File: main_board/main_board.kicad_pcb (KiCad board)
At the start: 2 copper layers, 80 x 80 mm, 103 parts, among them J10 B5B-XH, J11 B5B-XH, J12 B3B-XH, J13 B5B-XH, J2 Conn_01x02, J3 Conn_01x02, J4 EncSide, J5 MainSide, J6 EncSide, J7 MainSide, J8 Conn_01x02, J9 Conn_01x02, Q1 ST-1KL3A, Q10 DTC114E, Q2 ST-1KL3A, Q3 ST-1KL3A, Q4 ST-1KL3A, Q5 IRLML6344, Q6 IRLML6344, Q7 IRLML6344, Q8 IRLML6344, Q9 DTC114E, U1 ADCS7476, U10 AS5047D, U11 LSM6DSR, U12 OKL-T/6-W12N-C, U13 XC6221B302GR, U14 FT232RL, U15 SL2.1A, U2 BD63573NUV, U3 ADCS7476, U4 ADCS7476, U5 BD63573NUV, U6 ESP32-S3-PICO-1-N8R2, U7 AS5047D, U8 ADCS7476, U9 ADCS7476, Y1 12MHz

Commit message: アートワーク : 部品配置
Signed-off-by: Kazuki Iida <elkel53930@gmail.com>
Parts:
- D4, D5: footprint Library:SFH4550 -> Library:SFH4550_Mirror
- Q1, Q2: footprint Library:ST-1KL3A -> Library:ST-1KL3A_Mirror
- moved U9 186.0 mm to (215.0, 65.0), turned to 90 degrees
- moved C15 183.6 mm to (198.2, 140.5)
- moved C20 181.1 mm to (220.0, 75.5)
- moved C11 179.3 mm to (215.0, 68.0)
- moved C13 178.8 mm to (215.0, 69.5), turned to 180 degrees
- moved U1 178.1 mm to (207.0, 50.0), turned to 90 degrees
- moved C1 173.7 mm to (207.0, 53.0)
- moved C2 173.7 mm to (207.0, 54.5), turned to 180 degrees
- moved R10 170.3 mm to (215.0, 72.5), turned to 180 degrees
- moved R14 168.0 mm to (215.0, 74.0)
- moved R3 167.9 mm to (209.5, 53.0), turned to -90 degrees
- moved R18 165.3 mm to (215.0, 57.0)
- moved R5 164.0 mm to (209.5, 50.0), turned to -90 degrees
- moved U8 163.9 mm to (193.0, 54.5), turned to -90 degrees
- moved Q8 160.9 mm to (215.0, 60.0), turned to -90 degrees
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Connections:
- C31 pad 1: /Power/CHIP_PU -> CHIP_PU
- C33 pad 1: /Power/GPIO0 -> GPIO0
- Q10 pad 3: /Power/GPIO0 -> GPIO0
- Q9 pad 3: /Power/CHIP_PU -> CHIP_PU
- R1 pad 1: Net-(D1-K) -> /LED_0
- R1 pad 2: /LED_0 -> Net-(D1-K)
- R6 pad 1: /CHIP_PU -> CHIP_PU
- U14 pad 1: /Power/RXD0 -> RXD0
- U14 pad 5: /Power/TXD0 -> TXD0
- U6 pad 24: /CS_ENC_L -> /LED_1
- U6 pad 25: /CS_ENC_R -> unconnected-(U6-GPIO19-Pad25)
- U6 pad 38: /LED_1 -> /PWM_L
- U6 pad 39: /PWM_L -> /CWCCW_L
- U6 pad 4: /CHIP_PU -> CHIP_PU
- U6 pad 40: /CWCCW_L -> /CS_ENC_L
- U6 pad 41: /PWM_R -> /CS_ENC_R
- U6 pad 42: /CWCCW_R -> /PWM_R
- U6 pad 43: unconnected-(U6-GPIO38-Pad43) -> /CWCCW_R
- U6 pad 49: /TXD -> TXD0
- U6 pad 5: /GPIO0 -> GPIO0
- U6 pad 50: /RXD -> RXD0

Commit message: アートワーク : 部品配置完了
Signed-off-by: Kazuki Iida <elkel53930@gmail.com>
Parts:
- added G***: LOGO, Library:AMacLogo, F.Cu at (158.0, 44.5)
- added H1: M3 mounting hole, MountingHole:MountingHole_3.2mm_M3, F.Cu at (184.0, 116.5)
- added H10: M2 mounting hole, MountingHole:MountingHole_2.2mm_M2, F.Cu at (145.8, 82.8)
- added H11: M2 mounting hole, MountingHole:MountingHole_2.2mm_M2, F.Cu at (151.2, 82.8)
- added H2: M3 mounting hole, MountingHole:MountingHole_3.2mm_M3, F.Cu at (160.5, 61.3)
- added H3: M3 mounting hole, MountingHole:MountingHole_3.2mm_M3, F.Cu at (207.5, 61.3)
- added H4: M2 mounting hole, MountingHole:MountingHole_2.2mm_M2, F.Cu at (222.2, 95.2)
- added H5: M2 mounting hole, MountingHole:MountingHole_2.2mm_M2, F.Cu at (216.8, 95.2)
- added H6: M2 mounting hole, MountingHole:MountingHole_2.2mm_M2, F.Cu at (222.2, 82.8)
- added H7: M2 mounting hole, MountingHole:MountingHole_2.2mm_M2, F.Cu at (216.8, 82.8)
- added H8: M2 mounting hole, MountingHole:MountingHole_2.2mm_M2, F.Cu at (145.8, 95.2)
- added H9: M2 mounting hole, MountingHole:MountingHole_2.2mm_M2, F.Cu at (151.2, 95.2)
- moved C15 54.6 mm to (216.5, 89.0), turned to -90 degrees
- moved C16 53.7 mm to (151.5, 89.0), turned to -90 degrees
- moved D3 52.4 mm to (202.0, 83.5), turned to 90 degrees
- moved R2 51.0 mm to (202.0, 80.5), turned to 90 degrees
- moved U10 44.8 mm to (148.0, 89.0), turned to 90 degrees
- moved U7 43.8 mm to (220.0, 89.0), turned to 90 degrees
- moved J6 41.2 mm to (148.5, 100.0), turned to 180 degrees
- moved J4 39.7 mm to (219.5, 100.0), turned to 180 degrees
- moved R1 34.4 mm to (190.0, 62.0)
- moved D1 34.0 mm to (193.0, 62.0)
- moved R4 30.2 mm to (190.0, 60.5), turned to 180 degrees
- moved D2 30.1 mm to (193.0, 60.5)
- moved R6 14.3 mm to (183.0, 83.0), turned to 0 degrees
- moved C8 12.6 mm to (178.0, 63.5), turned to 0 degrees
- moved C23 4.00 mm to (189.0, 73.0)
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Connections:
- C15 pad 2: Net-(J4-Pin_6) -> Net-(J4-Pin_2)
- C16 pad 2: Net-(J6-Pin_6) -> Net-(J6-Pin_2)
- J5 pad 2: /SPI1_MOSI -> GND
- J5 pad 3: /SPI1_MISO -> /SPI1_MOSI
- J5 pad 4: /SPI1_SCK -> /SPI1_MISO
- J5 pad 5: /CS_ENC_L -> /SPI1_SCK
- J5 pad 6: GND -> /CS_ENC_L
- J7 pad 2: /SPI1_MOSI -> GND
- J7 pad 3: /SPI1_MISO -> /SPI1_MOSI
- J7 pad 4: /SPI1_SCK -> /SPI1_MISO
- J7 pad 5: /CS_ENC_R -> /SPI1_SCK
- J7 pad 6: GND -> /CS_ENC_R
- U10 pad 1: Net-(J6-Pin_5) -> Net-(J6-Pin_6)
- U10 pad 13: Net-(J6-Pin_6) -> Net-(J6-Pin_2)
- U10 pad 2: Net-(J6-Pin_4) -> Net-(J6-Pin_5)
- U10 pad 3: Net-(J6-Pin_3) -> Net-(J6-Pin_4)
- U10 pad 4: Net-(J6-Pin_2) -> Net-(J6-Pin_3)
- U10 pad 5: Net-(J6-Pin_6) -> Net-(J6-Pin_2)
- U6 pad 10: /LS_EN -> /SPI2_SCK
- U6 pad 11: /CS_BATT -> /CS_IMU
- U6 pad 12: /SPI2_MISO -> /PWM_R
- U6 pad 13: /SPI2_MOSI -> /CWCCW_R
- U6 pad 14: /SPI2_SCK -> /SPI1_MOSI
- U6 pad 15: /CS_IMU -> /SPI1_MISO
- U6 pad 16: /CS_LF -> /SPI1_SCK
- U6 pad 17: /LF_EN -> /CS_ENC_L
- U6 pad 18: /SPI1_MOSI -> /CS_ENC_R
- U6 pad 19: /SPI1_MISO -> /LED_0
- U6 pad 23: /SPI1_SCK -> /LED_1
- U6 pad 24: /LED_1 -> /CS_RF
- U6 pad 27: /LED_0 -> /RF_EN
- U6 pad 38: /PWM_L -> /CS_BATT
- U6 pad 39: /CWCCW_L -> /CS_RS
- U6 pad 40: /CS_ENC_L -> /RS_EN
- U6 pad 41: /CS_ENC_R -> /CS_LS
- U6 pad 42: /PWM_R -> /LS_EN
- U6 pad 43: /CWCCW_R -> /CS_LF
- U6 pad 52: /CS_RF -> /LF_EN
- U6 pad 6: /RF_EN -> /CWCCW_L
- U6 pad 7: /CS_RS -> /PWM_L
- U6 pad 8: /RS_EN -> /SPI2_MISO
- U6 pad 9: /CS_LS -> /SPI2_MOSI
- U7 pad 1: Net-(J4-Pin_5) -> Net-(J4-Pin_6)
- U7 pad 13: Net-(J4-Pin_6) -> Net-(J4-Pin_2)
- U7 pad 2: Net-(J4-Pin_4) -> Net-(J4-Pin_5)
- U7 pad 3: Net-(J4-Pin_3) -> Net-(J4-Pin_4)
- U7 pad 4: Net-(J4-Pin_2) -> Net-(J4-Pin_3)
- U7 pad 5: Net-(J4-Pin_6) -> Net-(J4-Pin_2)
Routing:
- net Net-(J4-Pin_1): track 0.00 -> 22.9 mm
- net Net-(J6-Pin_1): track 0.00 -> 19.9 mm
- net Net-(J6-Pin_2): track 0.00 -> 18.4 mm
- net Net-(J4-Pin_2): track 0.00 -> 17.8 mm
- net Net-(J6-Pin_6): track 0.00 -> 9.63 mm
- net Net-(J4-Pin_6): track 0.00 -> 9.22 mm
- net Net-(J6-Pin_5): track 0.00 -> 9.07 mm
- net Net-(J4-Pin_5): track 0.00 -> 8.74 mm
- net Net-(J6-Pin_3): track 0.00 -> 8.66 mm
- net Net-(J6-Pin_4): track 0.00 -> 8.51 mm
- net Net-(J4-Pin_3): track 0.00 -> 8.45 mm
- net Net-(J4-Pin_4): track 0.00 -> 8.39 mm
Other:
- outline, holes or cut-outs redrawn
- board text added: "TWILIGHT Main Board v1.0"

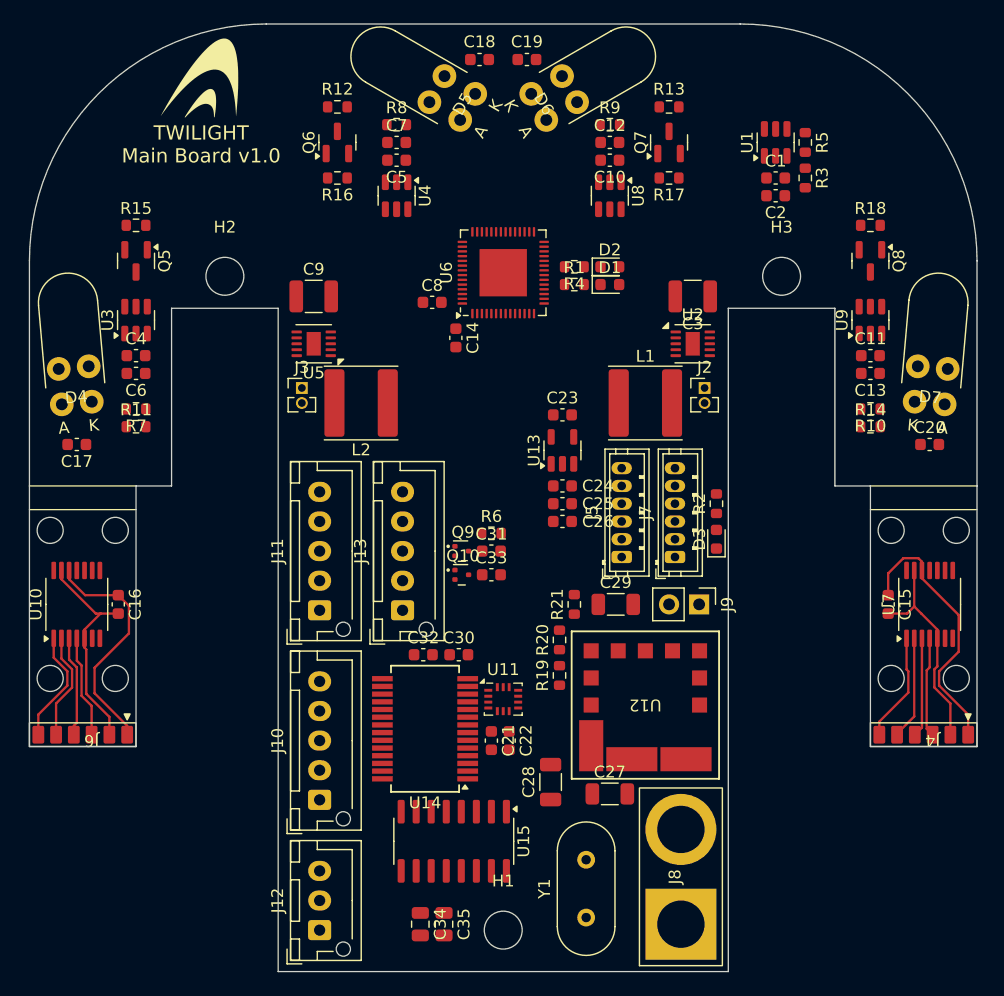
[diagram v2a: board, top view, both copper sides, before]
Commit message: アートワーク : 部品配置微修正
Signed-off-by: Kazuki Iida <elkel53930@gmail.com>
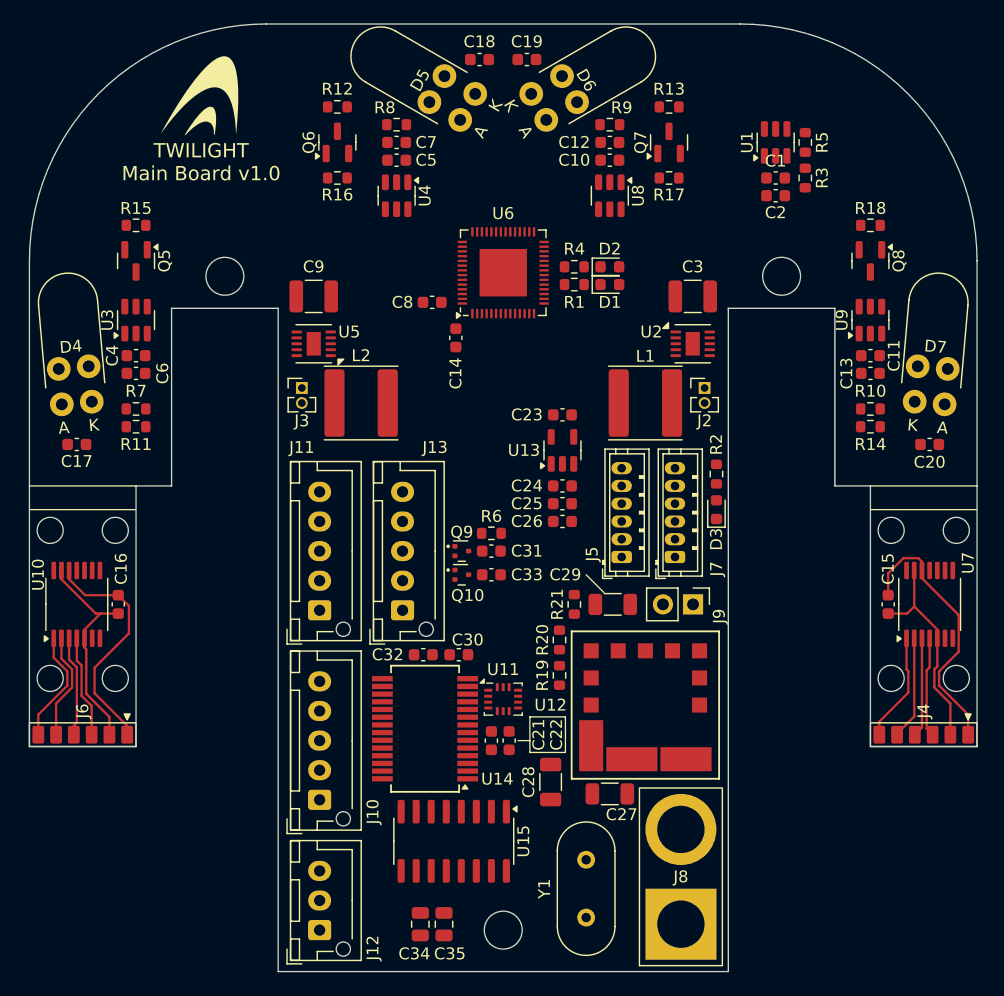
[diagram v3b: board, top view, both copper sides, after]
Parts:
- moved D3 2.50 mm to (202.0, 81.0)
- moved R2 2.50 mm to (202.0, 78.0)
- moved G*** 1.50 mm to (158.0, 46.0)
- moved J9 0.51 mm to (200.0, 89.0)
- moved C29 0.25 mm to (193.2, 89.0)

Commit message: アートワーク : 配線完了
Signed-off-by: Kazuki Iida <elkel53930@gmail.com>
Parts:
- removed H5, H9: M2 mounting hole, MountingHole:MountingHole_2.2mm_M2
- added C36: 1608 6.3V 10uF, Capacitor_SMD:C_0603_1608Metric, F.Cu at (176.5, 59.5)
- added C37: 1608 6.3V 10uF, Capacitor_SMD:C_0603_1608Metric, F.Cu at (180.0, 66.0)
- J10, J11, J13: footprint Connector_JST:JST_XH_B5B-XH-AM_1x05_P2.50mm_Vertical -> Connector_JST:JST_XH_B5B-XH-A_1x05_P2.50mm_Vertical
- J12: footprint Connector_JST:JST_XH_B3B-XH-AM_1x03_P2.50mm_Vertical -> Connector_JST:JST_XH_B3B-XH-A_1x03_P2.50mm_Vertical
- moved J13 17.5 mm to (168.5, 105.5)
- moved J10 17.4 mm to (175.2, 89.5)
- moved C14 12.0 mm to (185.8, 56.0), turned to 180 degrees
- moved U2 2.00 mm to (198.0, 67.0)
- moved U5 2.00 mm to (170.0, 67.0)
- moved C28 1.25 mm to (188.0, 105.2)
- turned C32 to 180 degrees
- turned R11 to 180 degrees
- turned R7 to 0 degrees
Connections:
- J12 pad 2: /Power/USB- -> /Power/USB+
- J12 pad 3: /Power/USB+ -> /Power/USB-
- U6 pad 12: /PWM_R -> /SPI1_MOSI
- U6 pad 13: /CWCCW_R -> /SPI1_MISO
- U6 pad 14: /SPI1_MOSI -> /SPI1_SCK
- U6 pad 15: /SPI1_MISO -> /CS_ENC_L
- U6 pad 16: /SPI1_SCK -> /CS_ENC_R
- U6 pad 17: /CS_ENC_L -> /PWM_R
- U6 pad 18: /CS_ENC_R -> /CWCCW_R
- U6 pad 39: /CS_RS -> /RS_EN
- U6 pad 40: /RS_EN -> /CS_RS
- U6 pad 6: /CWCCW_L -> /PWM_L
- U6 pad 7: /PWM_L -> /CWCCW_L
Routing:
- net +5V: track 0.00 -> 368.2 mm, vias 0 -> 11
- net +3V0: track 0.00 -> 309.2 mm, vias 0 -> 18
- net +BATT: track 0.00 -> 206.7 mm, vias 0 -> 4
- net /SPI2_MISO: track 0.00 -> 142.7 mm, vias 0 -> 7
- net /SPI2_SCK: track 0.00 -> 134.3 mm, vias 0 -> 6
- net TXD0: track 0.00 -> 56.9 mm, vias 0 -> 4
- net RXD0: track 0.00 -> 54.8 mm, vias 0 -> 4
- net /CS_LF: track 0.00 -> 37.8 mm
- net /SPI2_MOSI: track 0.00 -> 32.9 mm
- net /CS_RF: track 0.00 -> 32.7 mm, vias 0 -> 2
- net /CS_IMU: track 0.00 -> 32.7 mm
- net /Power/DP3: track 0.00 -> 32.5 mm
- net /RF_EN: track 0.00 -> 31.8 mm
- net /Power/DM3: track 0.00 -> 31.7 mm
- net /LF_EN: track 0.00 -> 30.9 mm
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- added copper zone on B.Cu, net GND
- added copper zone on F.Cu, net GND

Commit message: アートワーク : 微修正
Signed-off-by: Kazuki Iida <elkel53930@gmail.com>
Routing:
- net GND: track 2.31 -> 33.4 mm, vias 161 -> 135
- net /SPI2_SCK: track 134.3 -> 130.3 mm
- net /SPI2_MISO: track 142.7 -> 141.1 mm
- net /RS_EN: track 23.1 -> 23.8 mm
- net +3V0: track 309.2 -> 308.5 mm
- net /CS_LS: track 8.37 -> 9.05 mm
- net /CS_RS: track 16.3 -> 15.8 mm

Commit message: アートワーク : 微修正
Signed-off-by: Kazuki Iida <elkel53930@gmail.com>
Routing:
- net TXD0: track 56.9 -> 57.4 mm
- net GND: vias 135 -> 136

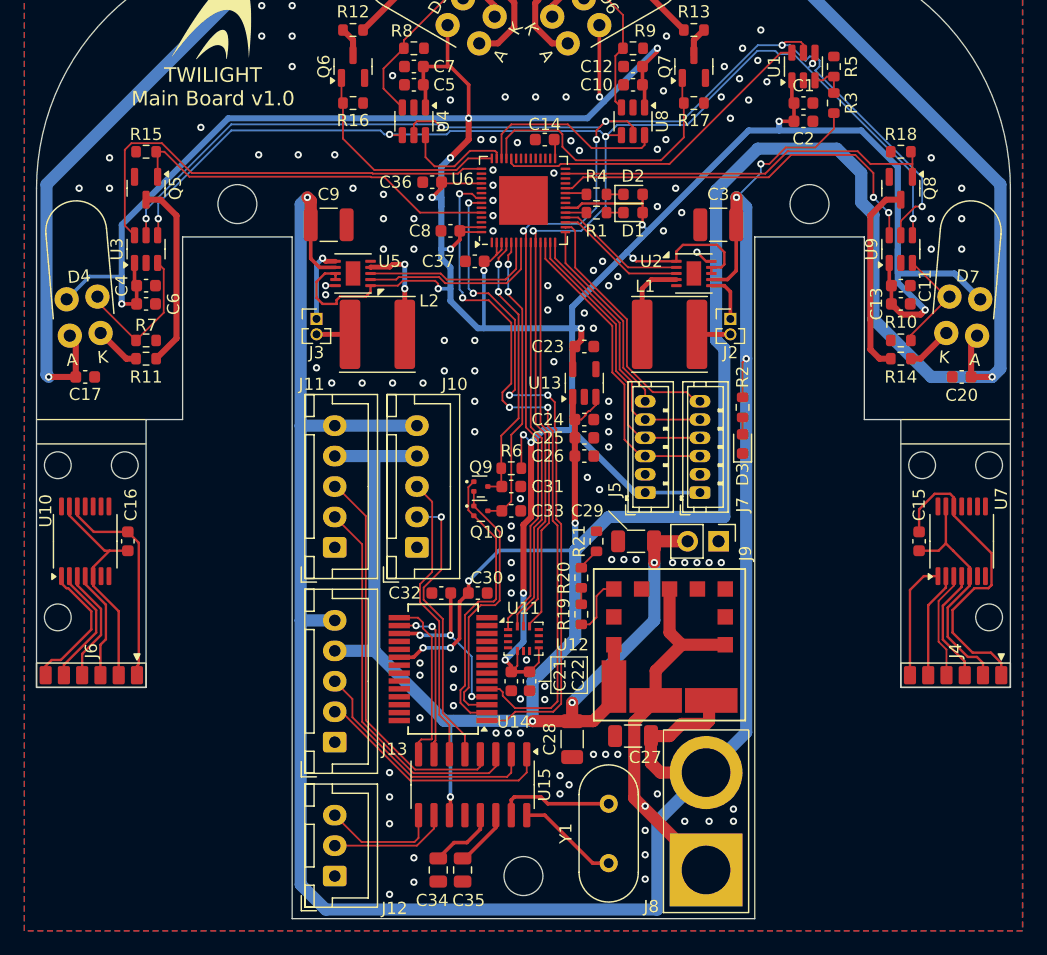
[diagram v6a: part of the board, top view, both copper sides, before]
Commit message: 回路図 : 3.0Vから3.3Vに変更 アートワーク : コネクタピン配などのシルクを追加
Signed-off-by: Kazuki Iida <elkel53930@gmail.com>
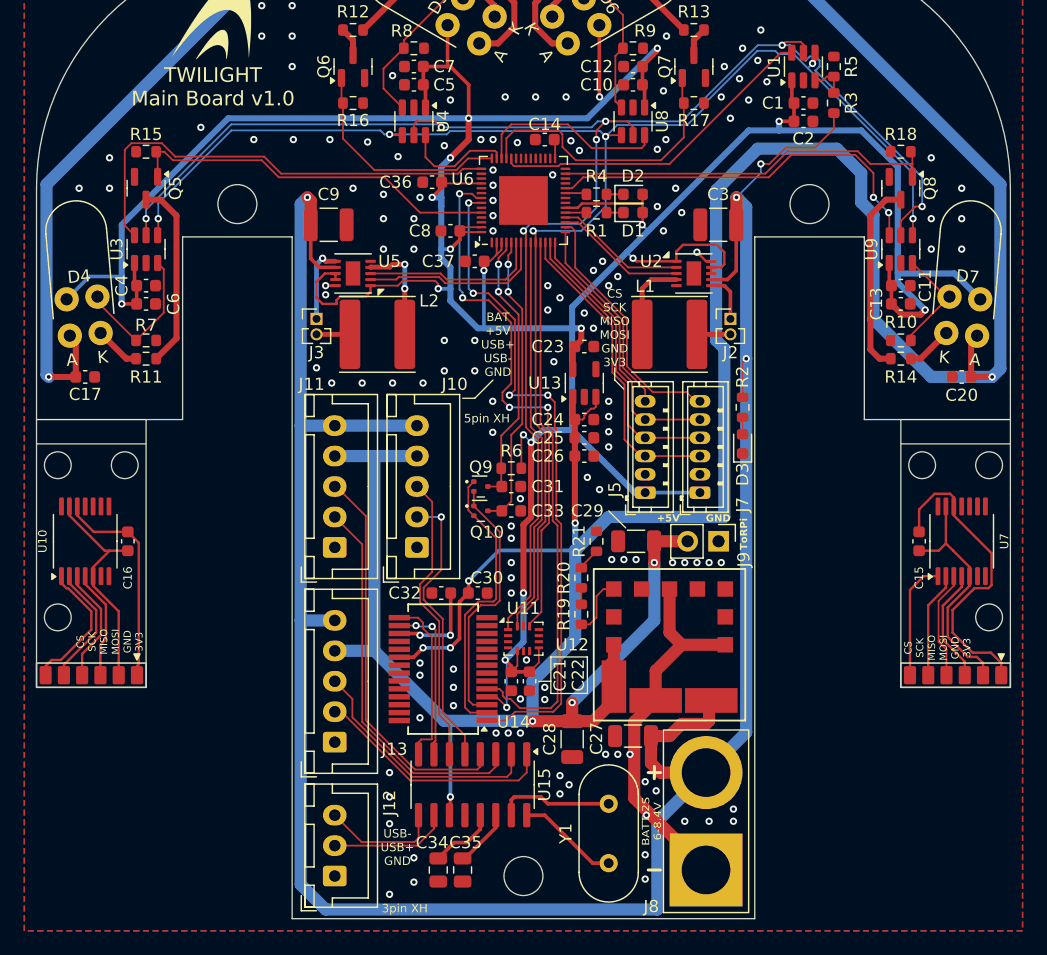
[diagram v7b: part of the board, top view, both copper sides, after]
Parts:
- U13: value XC6221B302GR -> XC6221B332MR
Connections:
- C1 pad 1: +3V0 -> +3V3
- C10 pad 1: +3V0 -> +3V3
- C11 pad 1: +3V0 -> +3V3
- C12 pad 2: +3V0 -> +3V3
- C13 pad 2: +3V0 -> +3V3
- C2 pad 2: +3V0 -> +3V3
- C21 pad 1: +3V0 -> +3V3
- C22 pad 1: +3V0 -> +3V3
- C23 pad 1: +3V0 -> +3V3
- C32 pad 1: +3V3 -> Net-(U14-3V3OUT)
- C36 pad 2: +3V0 -> +3V3
- C37 pad 2: +3V0 -> +3V3
- C4 pad 1: +3V0 -> +3V3
- C5 pad 1: +3V0 -> +3V3
- C6 pad 2: +3V0 -> +3V3
- C7 pad 2: +3V0 -> +3V3
- C8 pad 2: +3V0 -> +3V3
- D1 pad 2: +3V0 -> +3V3
- D2 pad 2: +3V0 -> +3V3
- J5 pad 1: +3V0 -> +3V3
- J7 pad 1: +3V0 -> +3V3
- Q1 pad 1: +3V0 -> +3V3
- Q2 pad 1: +3V0 -> +3V3
- Q3 pad 1: +3V0 -> +3V3
- Q4 pad 1: +3V0 -> +3V3
- R6 pad 2: +3V0 -> +3V3
- U1 pad 1: +3V0 -> +3V3
- U11 pad 5: +3V0 -> +3V3
- U11 pad 8: +3V0 -> +3V3
- U13 pad 5: +3V0 -> +3V3
- U14 pad 17: +3V3 -> Net-(U14-3V3OUT)
- U2 pad 1: +3V0 -> +3V3
- U2 pad 8: +3V0 -> +3V3
- U2 pad 9: +3V0 -> +3V3
- U3 pad 1: +3V0 -> +3V3
- U4 pad 1: +3V0 -> +3V3
- U5 pad 1: +3V0 -> +3V3
- U5 pad 8: +3V0 -> +3V3
- U5 pad 9: +3V0 -> +3V3
- U6 pad 2: +3V0 -> +3V3
- U6 pad 20: +3V0 -> +3V3
- U6 pad 3: +3V0 -> +3V3
- U6 pad 46: +3V0 -> +3V3
- U6 pad 55: +3V0 -> +3V3
- U6 pad 56: +3V0 -> +3V3
- U8 pad 1: +3V0 -> +3V3
- U9 pad 1: +3V0 -> +3V3
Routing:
- net +3V0: track 308.7 -> 0.00 mm, vias 18 -> 0
- net +3V3: track 14.7 -> 314.7 mm, vias 3 -> 19
- net Net-(U14-3V3OUT): track 0.00 -> 7.73 mm, vias 0 -> 2
- net /Power/RTS: track 22.0 -> 21.4 mm
- net GND: vias 136 -> 139
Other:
- board text added: "+5V"
- board text added: "3pin XH"
- board text added: "5pin XH"
- board text added: "BAT +5V USB+ USB- GND"
- board text added: "BATT 2S 6-8.4V"
- board text added: "CS SCK MISO MOSI GND 3V3"
- board text added: "GND"
- board text added: "ToRPi"
- board text added: "USB- USB+ GND"

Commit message: 微修正
Signed-off-by: Kazuki Iida <elkel53930@gmail.com>
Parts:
- moved D5 1.00 mm to (181.0, 48.0)
- moved D6 1.00 mm to (187.0, 48.0)
- moved Q2 1.00 mm to (181.0, 48.0)
- moved Q3 1.00 mm to (187.0, 48.0)
- moved R8 0.50 mm to (174.5, 48.5)
- moved R9 0.50 mm to (193.5, 48.5)
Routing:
- net +3V3: track 314.7 -> 310.6 mm
- net +5V: track 368.4 -> 366.3 mm
- net GND: vias 139 -> 146
